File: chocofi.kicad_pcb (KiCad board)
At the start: 2 copper layers, 112.5 x 90 mm, 57 parts, among them J1 MJ-4PP-9, J2 OLED, SW10 SW_PUSH, SW11 SW_PUSH, SW12 SW_PUSH, SW14 SW_PUSH, SW15 SW_PUSH, SW16 SW_PUSH, SW17 SW_PUSH, SW18 SW_PUSH, SW19 SW_PUSH, SW2 SW_PUSH, SW20 SW_PUSH, SW21 SW_PUSH, SW3 SW_PUSH, SW4 SW_PUSH, SW5 SW_PUSH, SW6 SW_PUSH, SW8 SW_PUSH, SW9 SW_PUSH, U1 ProMicro

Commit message: Fix refs
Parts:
- h3: renamed from h2; value h2 -> h3
- h4: renamed from h2; value h2 -> h4
- h5: renamed from h2; value h2 -> h5
- h6: renamed from h2; value h2 -> h6
- h7: renamed from h2; value h2 -> h7
- renumbered G*** to G1, G*** to G2

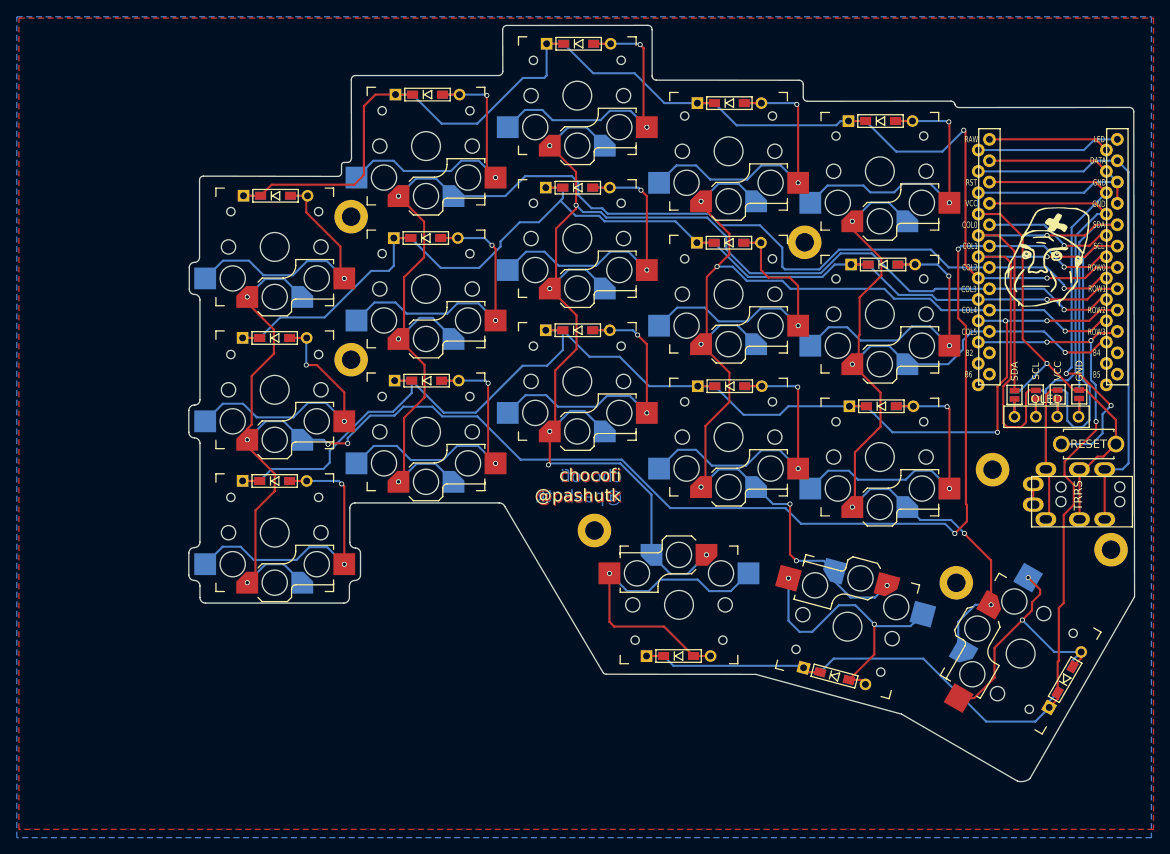
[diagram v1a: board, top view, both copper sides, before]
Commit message: Remove excessive corner pad surface, rm doorka logo
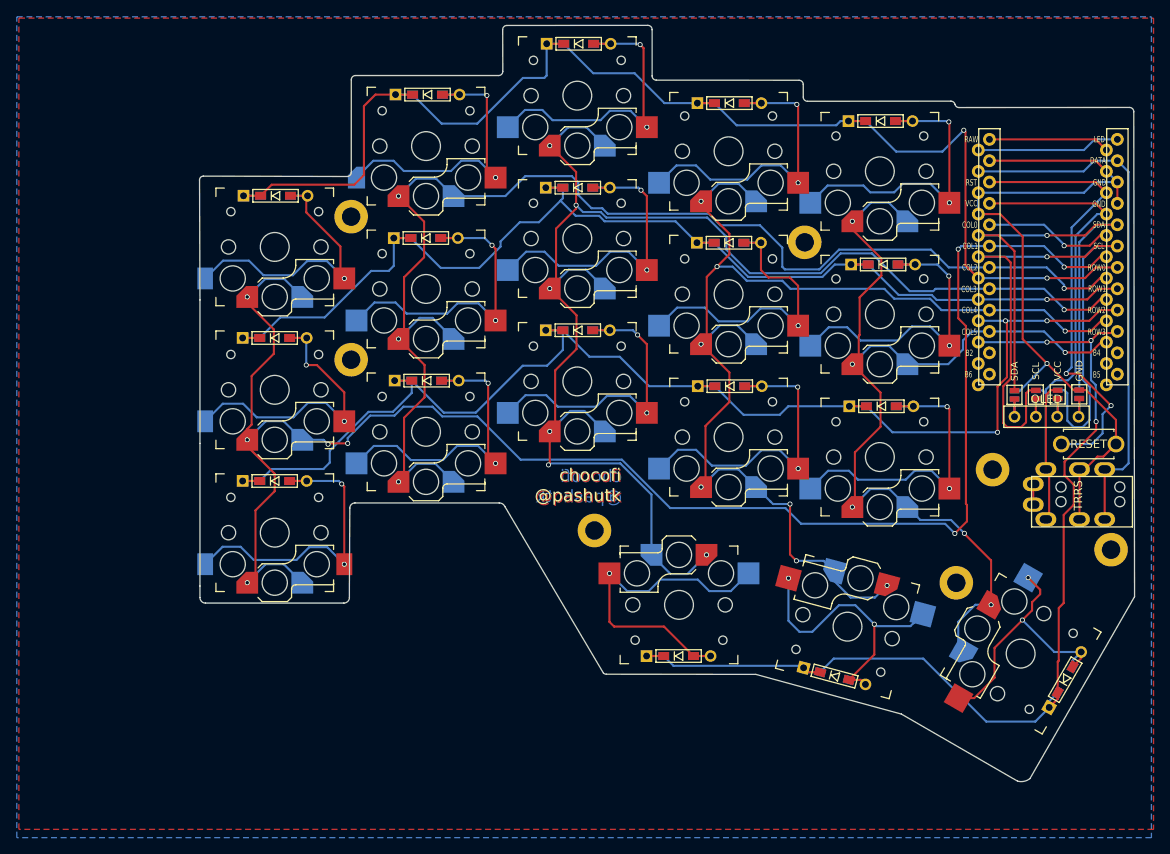
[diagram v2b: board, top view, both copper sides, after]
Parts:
- removed G1, G2: LOGO, my:doorka
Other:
- board size 112.5 x 90 mm -> 111.3 x 90 mm
